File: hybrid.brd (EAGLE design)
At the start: 161.3 x 168.9 mm, 125 parts, among them IC1 TL071P, IC2 TL071P, IC3 LM317MABT, IC4 LM317MABT, J1 RCJ-21XXMILL, J2 NRJ3HF-1, J3 703W-00/54, Q1 BC560KINKED, Q10 BC560KINKED, Q11 BC560KINKED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

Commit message: Horizontal version
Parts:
- removed H1: MOUNT-HOLE3.2, holes:3,2
- V1: value 6DJ8 -> (none); device my-tubes:NOVAL-21MM -> my-tubes:NOVAL-HORIZONTAL
- moved R28 26.8 mm to (114.3, 55.9), turned to 90 degrees
- moved R27 26.1 mm to (118.1, 55.9), turned to 90 degrees
- moved R25 24.5 mm to (116.8, 33.0)
- moved C16 23.3 mm to (116.8, 44.5)
- moved R9 22.9 mm to (81.3, 55.9), turned to 90 degrees
- moved C6 20.4 mm to (78.7, 44.5)
- moved R8 19.7 mm to (77.5, 55.9), turned to 90 degrees
- moved C14 19.2 mm to (116.8, 21.6)
- moved R6 13.5 mm to (78.7, 33.0)
- moved C13 12.7 mm to (149.9, 54.6)
- moved H2 12.7 mm to (166.4, 87.6)
- moved IC2 12.7 mm to (148.6, 68.6)
- moved J1 12.7 mm to (170.2, 20.3)
- moved Q16 12.7 mm to (149.9, 15.2)
- moved Q18 12.7 mm to (149.9, 2.54)
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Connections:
- net +6.3FIL: now also V1.7, V1.8; no longer V1.4
- net CAT_L: now also V1.2; no longer V1.3
- net CAT_R: now also V1.16; no longer V1.8
- net FGND: now also V1.10, V1.9; no longer V1.5
- net GND: now also V1.11, V1.12, V1.14, V1.4, V1.5, V1.6
- net G_L: now also V1.3; no longer V1.2
- net G_R: now also V1.13; no longer V1.7
- net PL_R: now also V1.15; no longer V1.6
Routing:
- net FGND: track 57.7 -> 37.2 mm, vias 2 -> 1
- net IN_R: track 137.9 -> 155.5 mm, vias 1 -> 2
- net VCC: track 554.9 -> 570.7 mm, vias 3 -> 7
- net FB_L: track 81.8 -> 96.3 mm, vias 3 -> 4
- net FB_R: track 81.8 -> 96.3 mm, vias 3 -> 4
- net G_R: track 26.3 -> 39.6 mm, vias 1 -> 0
- net OUT_R: track 152.1 -> 164.8 mm
- net +6.3FIL: track 59.8 -> 47.4 mm, vias 2 -> 1
- net CAT_R: track 24.1 -> 12.5 mm
- net IN_L: track 126.8 -> 117.2 mm
- net PL_R: track 31.9 -> 40.4 mm
- net IN_R*: track 196.6 -> 201.4 mm
- net IN_L*: track 207.4 -> 212.2 mm
- net CAT_L: track 17.1 -> 12.5 mm
- net AC_1: track 53.1 -> 56.9 mm
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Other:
- board size 161.3 x 168.9 mm -> 174 x 168.9 mm

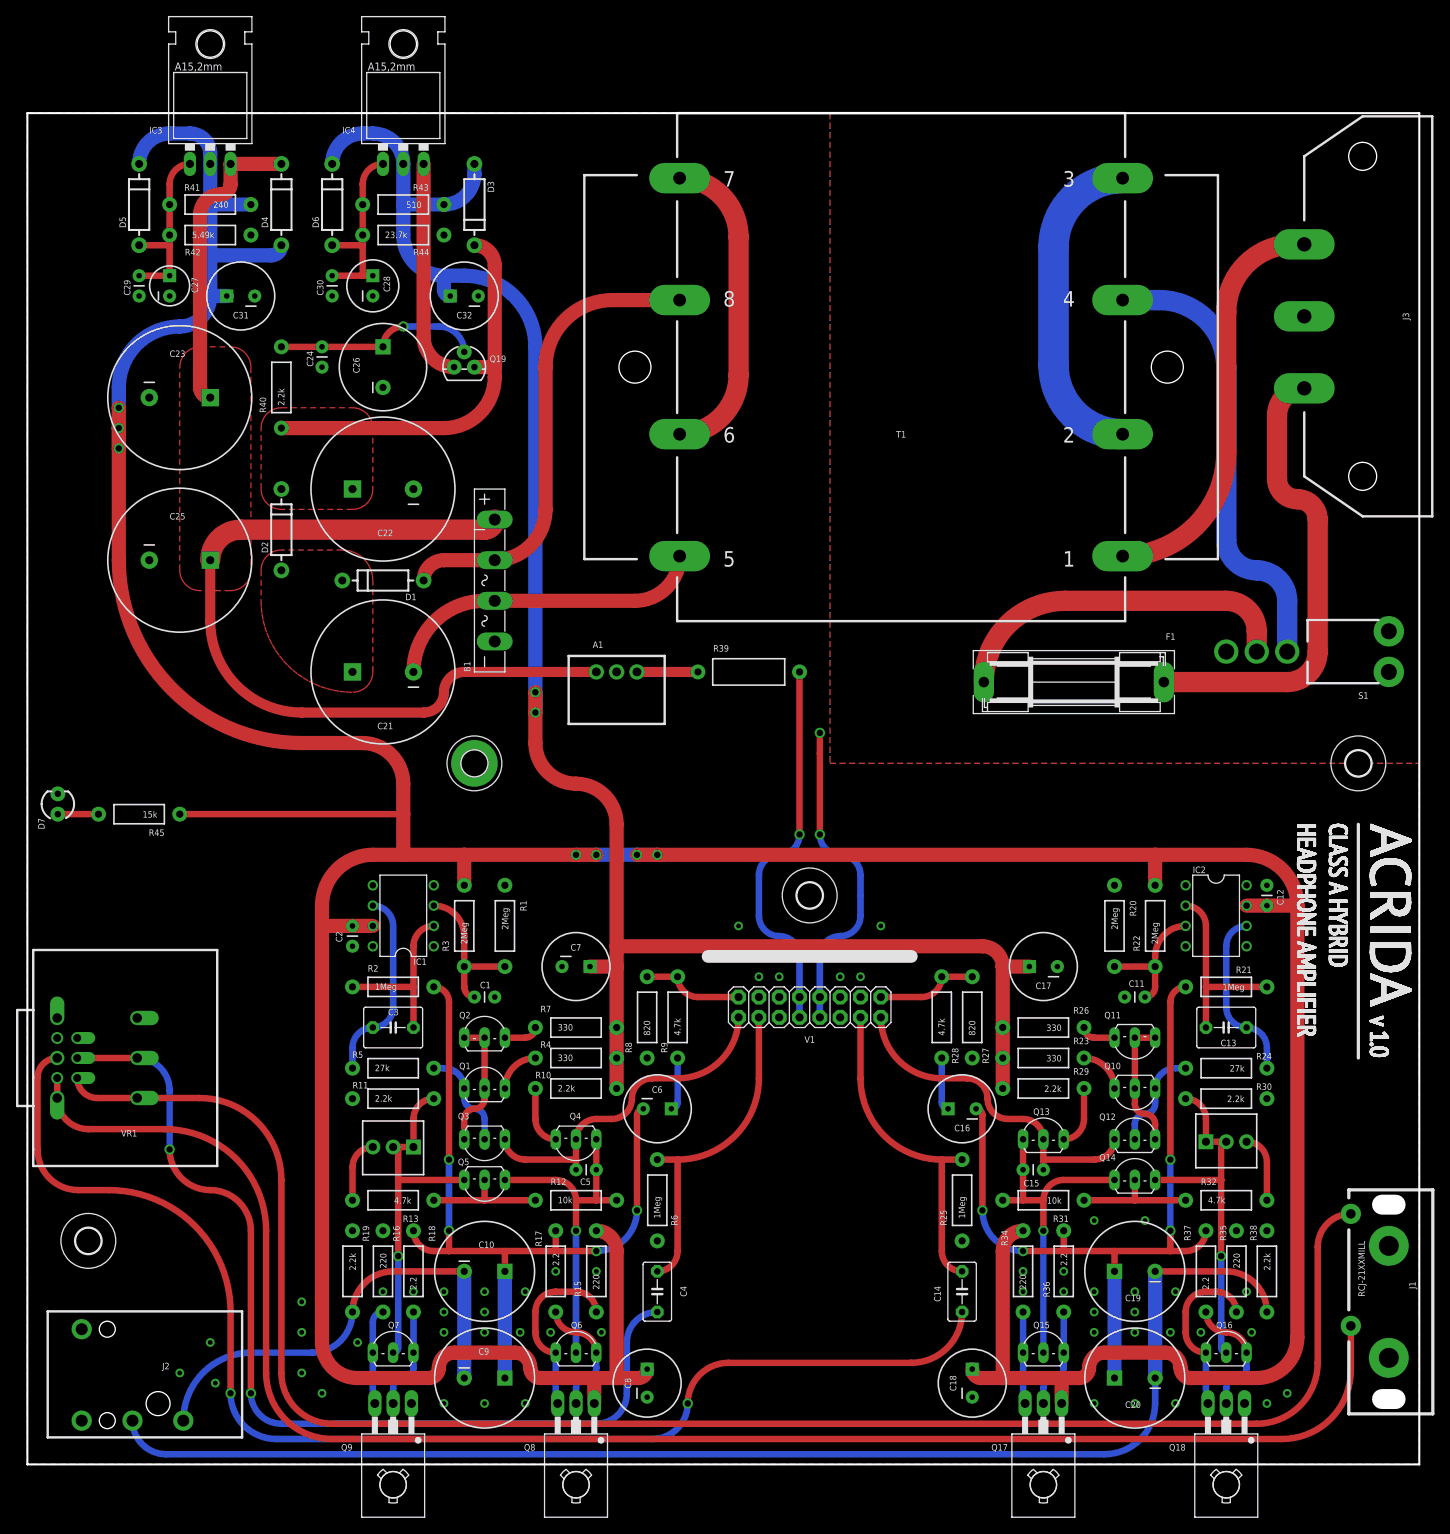
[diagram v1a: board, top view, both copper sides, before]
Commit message: A bit more room for tube cooling
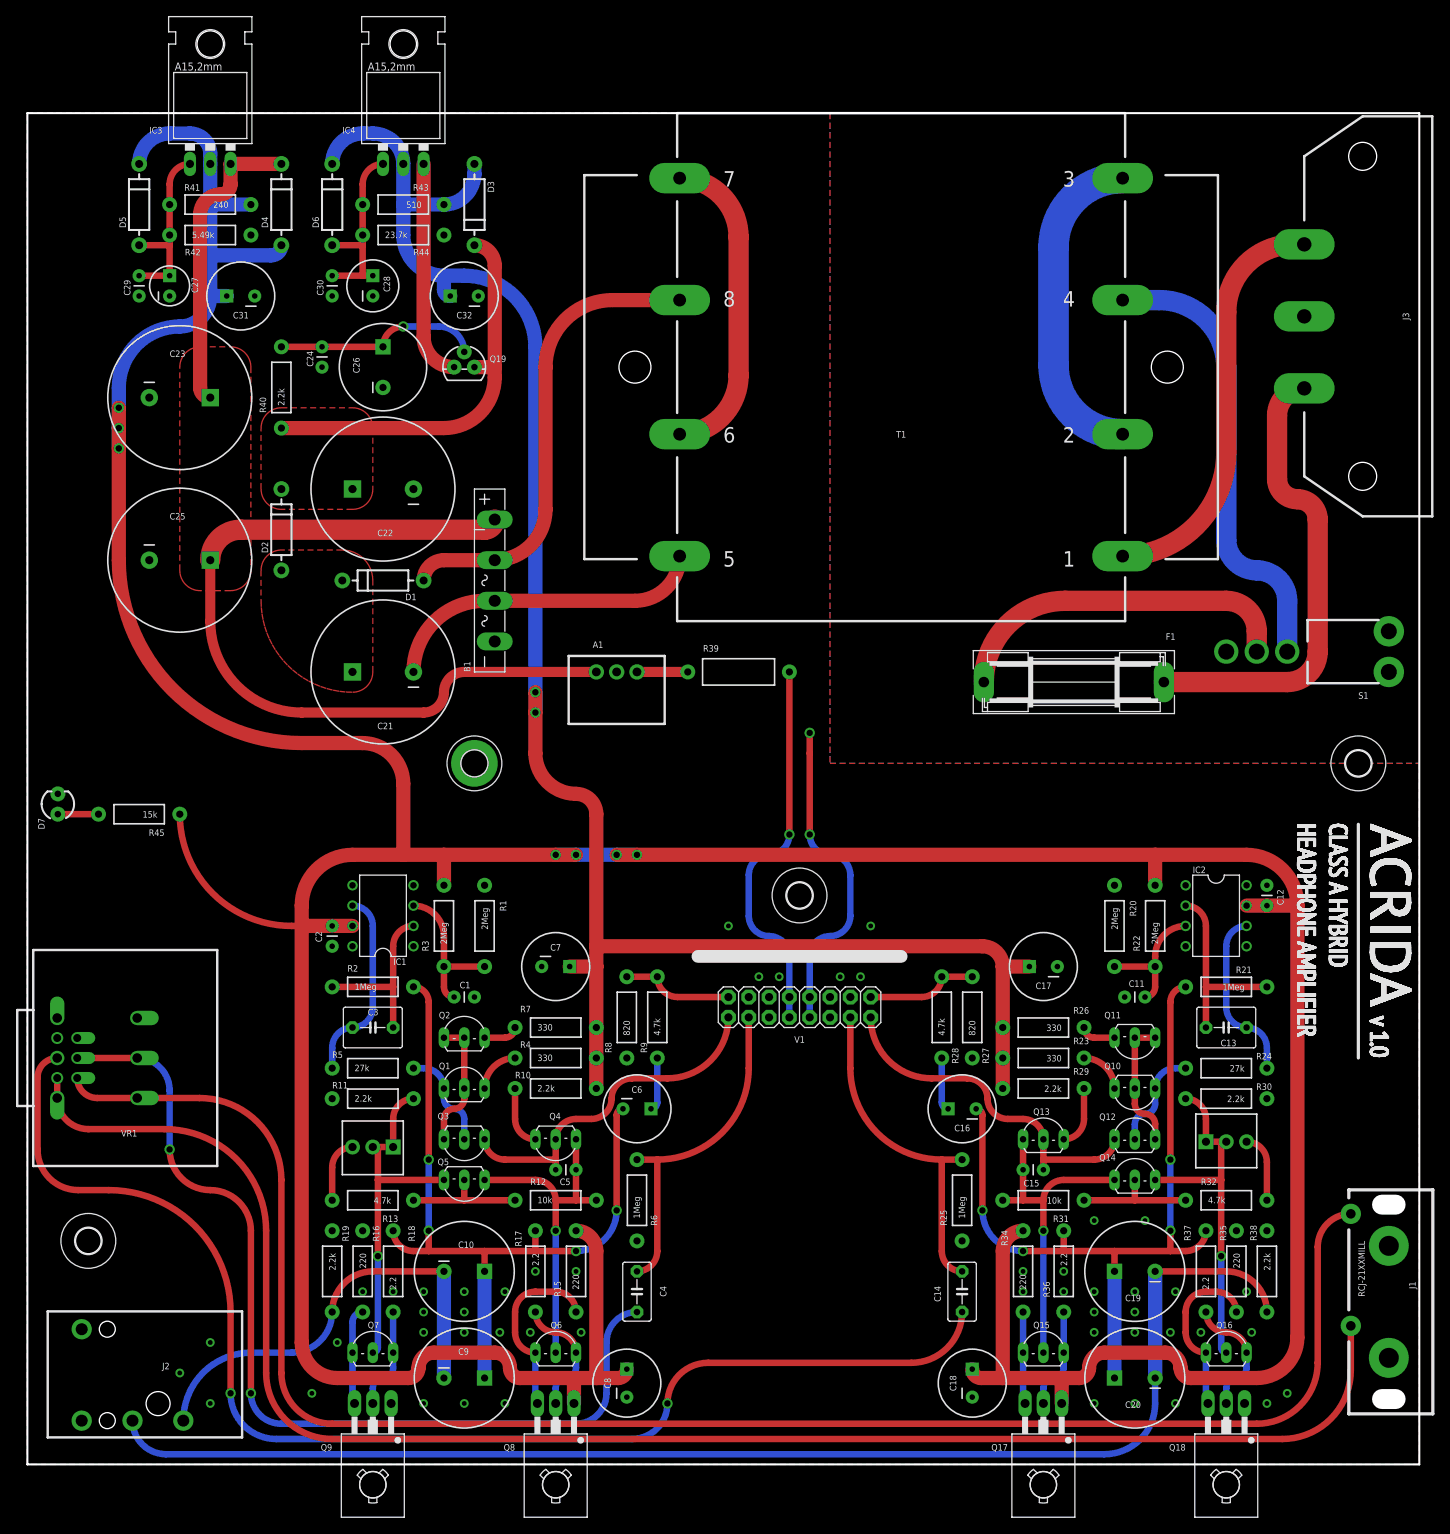
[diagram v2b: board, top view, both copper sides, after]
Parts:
- moved R15 2.54 mm to (68.6, 24.1)
- moved R16 2.54 mm to (41.9, 24.1)
- moved R17 2.54 mm to (63.5, 24.1)
- moved R9 2.54 mm to (78.7, 55.9)
- moved C1 2.54 mm to (55.9, 58.4)
- moved C10 2.54 mm to (54.6, 24.1)
- moved C2 2.54 mm to (38.1, 64.8)
- moved C3 2.54 mm to (43.2, 54.6)
- moved C9 2.54 mm to (54.6, 10.8)
- moved IC1 2.54 mm to (44.5, 68.6)
- moved Q1 2.54 mm to (54.6, 48.3)
- moved Q2 2.54 mm to (54.6, 54.6)
- moved Q3 2.54 mm to (54.6, 39.4)
- moved Q5 2.54 mm to (54.6, 34.3)
- moved Q7 2.54 mm to (43.2, 15.2)
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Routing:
- net VCC: track 570.7 -> 566.4 mm
- net OUT_L: track 56.2 -> 53.6 mm
- net IN_L: track 117.2 -> 114.6 mm
- net HT: track 228.5 -> 230.0 mm
- net CAT_R: track 12.5 -> 13.8 mm
- net PL_R: track 40.4 -> 41.7 mm
- net PL_L: track 40.4 -> 41.7 mm
- net N$32: track 7.62 -> 6.35 mm
- net CAT_L: track 12.5 -> 13.8 mm
- net G_R: track 39.6 -> 40.1 mm
- net G_L: track 39.6 -> 40.1 mm
- net GND: vias 54 -> 51

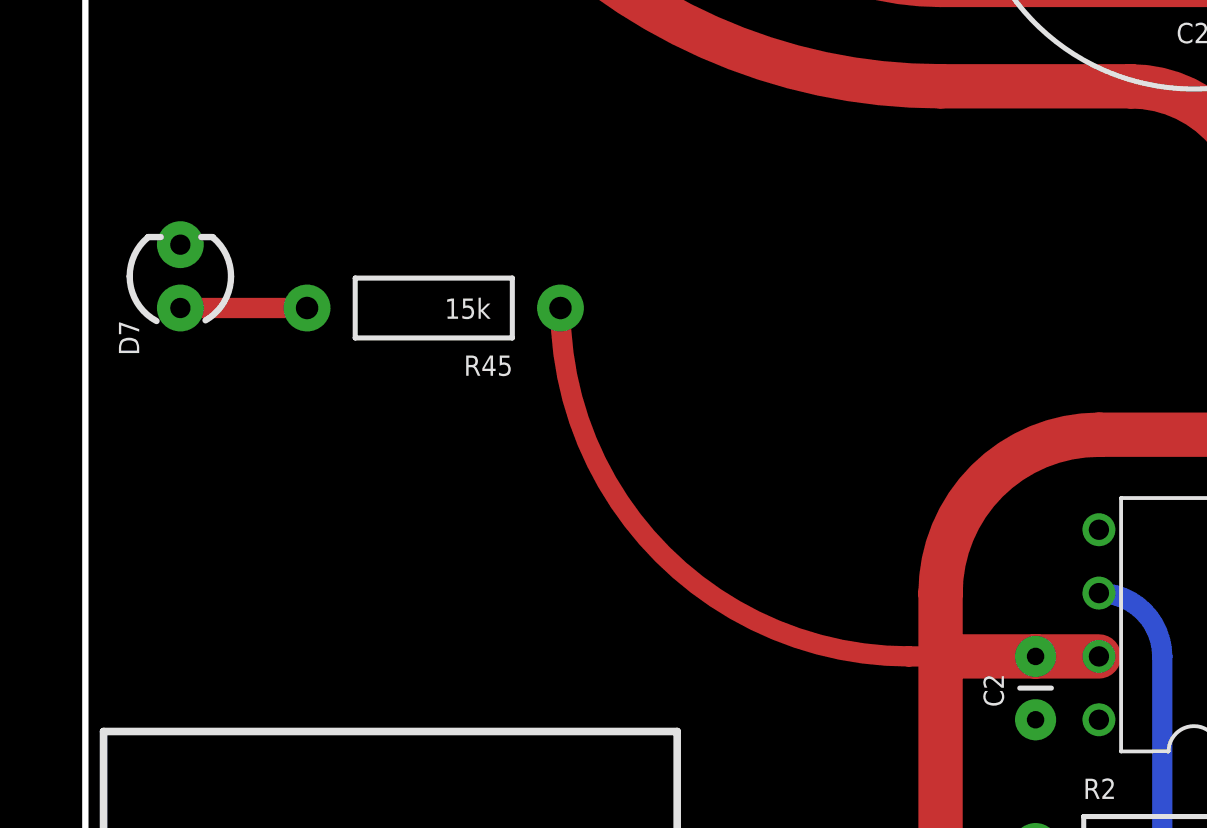
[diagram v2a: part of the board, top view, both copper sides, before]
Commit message: Move LED to canter
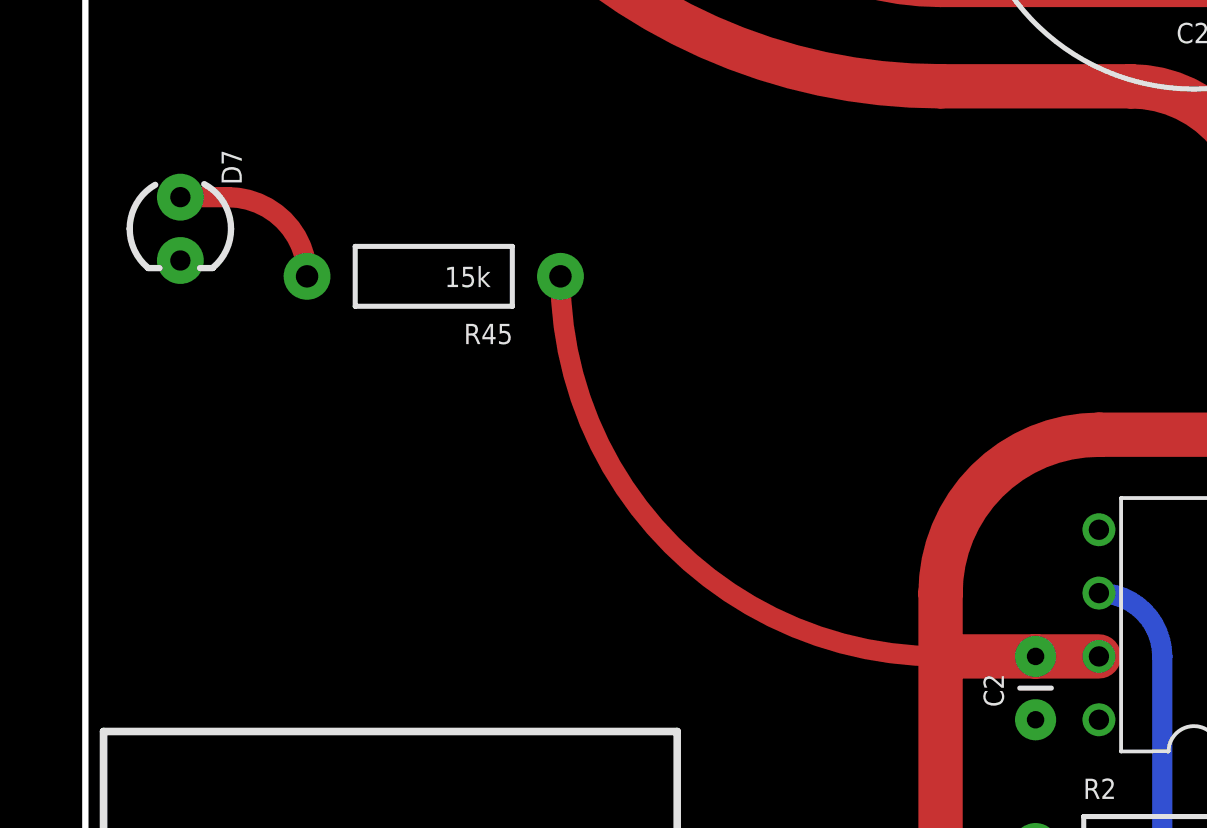
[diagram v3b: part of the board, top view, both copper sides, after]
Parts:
- moved D7 1.91 mm to (3.81, 84.5), turned to 270 degrees
- moved R45 1.27 mm to (14.0, 82.5)
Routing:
- net N$46: track 5.08 -> 6.40 mm
- net VCC: track 566.4 -> 566.9 mm
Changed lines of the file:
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@@
 <element name="H4" library="holes" package="3,2-PAD" value="MOUNT-PAD-ROUND3.2" x="55.88" y="87.63" smashed="yes"/>
 <element name="H5" library="holes" package="3,2" value="MOUNT-HOLE3.2" x="7.62" y="27.94" smashed="yes"/>
-<element name="D7" library="SparkFun-LED" package="LED3MM" value="" x="3.81" y="82.55" smashed="yes" rot="R90">
-<attribute name="PROD_ID" value="DIO-08794" x="3.81" y="82.55" size="1.778" layer="27" rot="R90" display="off"/>
-<attribute name="NAME" x="2.159" y="79.375" size="0.8128" layer="25" ratio="20" rot="R90"/>
-<attribute name="VALUE" x="5.461" y="84.455" size="1.27" layer="27" ratio="10" rot="R90"/>
+<element name="D7" library="SparkFun-LED" package="LED3MM" value="" x="3.81" y="84.455" smashed="yes" rot="R270">
+<attribute name="PROD_ID" value="DIO-08794" x="3.81" y="84.455" size="1.778" layer="27" rot="R270" display="off"/>
+<attribute name="NAME" x="5.461" y="87.63" size="0.8128" layer="25" ratio="20" rot="R270"/>
+<attribute name="VALUE" x="2.159" y="82.55" size="1.27" layer="27" ratio="10" rot="R270"/>
 </element>
-<element name="R45" library="SparkFun-Resistors" package="AXIAL-0.4" value="15k" x="13.97" y="81.28" smashed="yes" rot="R180">
-<attribute name="NAME" x="17.145" y="79.375" size="0.8128" layer="25" font="vector" ratio="20" rot="R180"/>
-<attribute name="VALUE" x="16.256" y="81.661" size="0.8128" layer="21" font="vector" ratio="20" rot="R180"/>
+<element name="R45" library="SparkFun-Resistors" package="AXIAL-0.4" value="15k" x="13.97" y="82.55" smashed="yes" rot="R180">
+<attribute name="NAME" x="17.145" y="80.645" size="0.8128" layer="25" font="vector" ratio="20" rot="R180"/>
+<attribute name="VALUE" x="16.256" y="82.931" size="0.8128" layer="21" font="vector" ratio="20" rot="R180"/>
 </element>
 <element name="U$1" library="my-logo" package="ACRIDA-LOGO" value="ACRIDA-LOGO" x="158.75" y="80.01" smashed="yes" rot="R270"/>
@@
 <wire x1="30.48" y1="151.13" x2="22.86" y2="151.13" width="1.778" layer="16"/>
 <wire x1="40.64" y1="67.31" x2="38.1" y2="67.31" width="1.778" layer="1"/>
-<wire x1="34.29" y1="67.31" x2="38.1" y2="67.31" width="1.778" layer="1"/>
+<wire x1="38.1" y1="67.31" x2="34.29" y2="67.31" width="1.778" layer="1"/>
 <wire x1="34.29" y1="67.31" x2="34.29" y2="15.24" width="1.778" layer="1"/>
 <wire x1="34.29" y1="15.24" x2="38.735" y2="10.795" width="1.778" layer="1" curve="90"/>
@@
 <wire x1="34.29" y1="90.17" x2="41.91" y2="90.17" width="1.778" layer="1"/>
 <wire x1="46.99" y1="85.09" x2="46.99" y2="76.2" width="1.778" layer="1"/>
-<wire x1="19.05" y1="81.28" x2="33.02" y2="67.31" width="0.8128" layer="1" curve="90"/>
-<wire x1="33.02" y1="67.31" x2="34.29" y2="67.31" width="0.8128" layer="1"/>
+<wire x1="34.29" y1="67.31" x2="19.05" y2="82.55" width="0.8128" layer="1" curve="-90"/>
 </signal>
 <signal name="OUT_L" class="1">
@@
 <contactref element="D7" pad="A"/>
 <contactref element="R45" pad="P$2"/>
-<wire x1="8.89" y1="81.28" x2="3.81" y2="81.28" width="0.8128" layer="1"/>
+<wire x1="3.81" y1="85.725" x2="5.715" y2="85.725" width="0.8128" layer="1"/>
+<wire x1="5.715" y1="85.725" x2="8.89" y2="82.55" width="0.8128" layer="1" curve="-90"/>
 </signal>
 </signals>

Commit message: Snap in cap
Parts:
- removed C25: 2200uF, my-cap:CPOL-RADIAL-18/7.5
- C23: value 2200uF -> 4700uF; device my-cap:CPOL-RADIAL-18/7.5 -> my-cap:CPOL-SNAPIN-30/10
- moved C23 8.03 mm to (16.5, 125.7)
- moved C31 2.54 mm to (24.1, 146.1)
- moved C27 2.54 mm to (15.2, 147.3)
- moved C29 2.54 mm to (11.4, 148.6)
- moved D5 2.54 mm to (11.4, 157.5)
- moved B1 2.54 mm to (61.0, 110.5)
- moved C21 2.54 mm to (47.0, 99.1)
- moved C22 2.54 mm to (47.0, 121.9)
- moved C24 2.54 mm to (39.4, 139.7)
- moved C26 2.54 mm to (47.0, 137.2)
- moved C28 2.54 mm to (45.7, 147.3)
- moved C30 2.54 mm to (40.6, 148.6)
- moved C32 2.54 mm to (57.1, 146.1)
- moved D1 2.54 mm to (47.0, 110.5)
- moved D2 2.54 mm to (34.3, 116.8)
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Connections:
- net +LV: no longer C25.1
- net GND: no longer C25.2
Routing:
- net +LV: track 138.0 -> 152.3 mm
- net AC_1: track 56.9 -> 54.4 mm
- net AC_2: track 39.3 -> 36.7 mm
- net HT: track 230.0 -> 228.9 mm
- removed copper zone on layer 1, net +LV

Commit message: No silk for vregs
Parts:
- IC3, IC4: value LM317MABT -> LM317MABT-OUT; device v-reg:TO220L1 -> my-reg:TO220L1-OUT
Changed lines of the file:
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@@
 <attribute name="VALUE" x="147.955" y="72.136" size="0.8128" layer="27" ratio="20" rot="R270"/>
 </element>
-<element name="IC3" library="v-reg" package="TO220L1" value="LM317MABT" x="20.32" y="166.37" smashed="yes">
+<element name="IC3" library="my-reg" package="TO220L1-OUT" value="LM317MABT-OUT" x="20.32" y="166.37" smashed="yes">
 <attribute name="NAME" x="12.7" y="166.37" size="0.8128" layer="25" ratio="20"/>
 <attribute name="VALUE" x="16.383" y="168.91" size="0.8128" layer="27" ratio="20"/>
 </element>
-<element name="IC4" library="v-reg" package="TO220L1" value="LM317MABT" x="49.53" y="166.37" smashed="yes">
+<element name="IC4" library="my-reg" package="TO220L1-OUT" value="LM317MABT-OUT" x="49.53" y="166.37" smashed="yes">
 <attribute name="NAME" x="41.91" y="166.37" size="0.8128" layer="25" ratio="20"/>
 <attribute name="VALUE" x="45.593" y="168.91" size="0.8128" layer="27" ratio="20"/>
